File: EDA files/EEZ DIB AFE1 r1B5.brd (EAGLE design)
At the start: 141.5 x 68.5 mm, 198 parts, among them IC1 MCP6004T-I/ST, IC10 N.C., IC11 N.C., IC12 N.C., IC13 ADS131E04IPAGR, IC14 TPS71725DCKR, IC15 TPS72325DBVR, IC2 DG212BDY-T1-E3, IC3 ULN2803ADWR, IC4 MCP6004T-I/ST, IC5 DG212BDY-T1-E3, IC6 TLV9001IDBVR, IC7 DG212BDY-T1-E3, IC8 TLV9001IDBVR, IC9 DG212BDY-T1-E3, Q1 CPC3902ZTR, Q2 CPC3902ZTR, Q3 CPC3902ZTR, Q4 CPC3902ZTR, Q5 BSS214NH6327XTSA1, Q6 BSS214NH6327XTSA1, Q7 BSS214NH6327XTSA1, Q8 BSS214NH6327XTSA1, X1 691322310008, X2 DS1023-2*14S21, X3 DS1023-2*14S21

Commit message: #1, #2, BOM (r1B5)
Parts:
- removed C28A: N.C., EEZ_Lib1:C050-075X110
- removed C36, C37, C42, C47, C48: 1u, rcl:C0805
- removed C38, C39, C40, C41: 470p, rcl:C0603
- removed C43, C44, C45, C46, C49, C50, C51: 100n, rcl:C0603
- removed C52: 10u, rcl:C1206
- removed IC14: TPS71725DCKR, EEZ_TI:DCK5
- removed IC15: TPS72325DBVR, EEZ_TI:DBV5
- removed JP7: JP2-CUT-0805, EEZ_Lib1:R_0805
- removed R55, R56, R57, R58, R59, R60, R61: 1K, rcl:R0805
- removed R62, R63: 10K, rcl:R0805
- removed R64, R65: 10R, rcl:R1206
- added XO1: N.C., EEZ_DIB:XLH
- C12: value N.C. -> 10u; device rcl:C0805 -> rcl:C1206
- C17: value 470p -> 22u; device rcl:C0603 -> rcl:C1206
- C18: value 470p -> 10u; device rcl:C0603 -> rcl:C1206
- C19: value 470p -> N.C.; device rcl:C0603 -> EEZ_Lib1:EC1206
- C20: value 470p -> N.C.; device rcl:C0603 -> EEZ_Lib1:C050-075X110
- C21: value 22u -> 100n; device rcl:C1206 -> rcl:C0603
- C22: value 10u -> 100n; device rcl:C1206 -> rcl:C0603
- C23: value N.C. -> 1u; device rcl:C0603 -> rcl:C0805
- C24, C25: value N.C. -> 1u; device rcl:C1206 -> rcl:C0805
- C26, C27: value N.C. -> 100n; device rcl:C1206 -> rcl:C0603
- C28: value N.C. -> 100n; device EEZ_Lib1:EC1206 -> rcl:C0603
- C29: value N.C. -> 100n
- C30, C31: value 15n -> 1u; device rcl:C0603 -> rcl:C0805
- C32, C33: value 15n -> 100n
- C35: value 100n -> 10u; device rcl:C0603 -> rcl:C1206
- F3, F5: value ZH32 (10A) -> ZH32 (1.25A)
- F4, F6: value ZH32 (1A) -> ZH32 (10A)
- IC11: value N.C. -> ADS131E04IPAGR; device EEZ_TI:DBV5 -> EEZ_TI:PAG64
- IC12: value N.C. -> TPS71725DCKR; device EEZ_TI:SOIC127P600X175-8N -> EEZ_TI:DCK5
- IC13: value ADS131E04IPAGR -> TPS72325DBVR; device EEZ_TI:PAG64 -> EEZ_TI:DBV5
- R1, R18: value 47R -> 15R
- R33, R43: value 0R33 -> GMR100HTBFIR022; device rcl:R1210 -> EEZ_Lib1:R_2512-4WIRE
- R51, R52: value N.C. -> 10K
- R53: value N.C. -> 10R; device rcl:R0805 -> rcl:R1206
- R54: value 1K -> 10R; device rcl:R0805 -> rcl:R1206
- moved R53 41.7 mm to (73.9, 18.2), turned to 90 degrees
- moved C24 40.6 mm to (71.1, 14.7), turned to 180 degrees
- moved C25 39.6 mm to (77.0, 16.7)
- moved C26 39.5 mm to (77.4, 18.6), turned to 180 degrees
- moved C35 36.7 mm to (101.1, 27.8), turned to 0 degrees
- moved C28 36.1 mm to (82.9, 26.2), turned to 90 degrees
- moved C23 35.2 mm to (75.1, 14.7)
- moved IC12 34.3 mm to (74.8, 11.4)
- moved C8 32.6 mm to (117.2, 65.6), turned to 180 degrees
- moved C20 32.5 mm to (111.9, 14.1)
- moved C34 31.4 mm to (100.2, 25.8)
- moved C19 30.4 mm to (108.5, 9.03), turned to 180 degrees
- moved R51 25.2 mm to (82.0, 14.1), turned to 180 degrees
- moved C27 22.5 mm to (101.9, 24.1), turned to 0 degrees
- moved F3 22.2 mm to (47.9, 46.6)
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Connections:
- removed net IN1+: C20.2, C30.2, IC13.16, R54.2
- removed net IN1-: C19.2, C30.1, IC13.15, R55.2
- removed net IN2+: C18.2, C31.2, IC13.14, R56.2
- removed net IN2-: C17.2, C31.1, IC13.13, R57.2
- removed net IN3+: C32.2, C38.2, IC13.12, R58.2
- removed net IN3-: C32.1, C39.2, IC13.11, R59.2
- removed net IN4+: C33.2, C40.2, IC13.10, R60.2
- removed net IN4-: C33.1, C41.2, IC13.9, R61.2
- removed net N$100: C27.1, C28.+, C28A.1, IC10.6, IC10.7, IC12.6, JP5.NC, R53.2
- removed net N$101: C25.1, C26.1, IC11.3, R53.1
- removed net N$102: C12.2, IC11.4, R51.2
- removed net N$103: C12.1, IC11.1, R52.2
- removed net N$104: JP5.NO, R51.1, R52.1
- removed net N$141: F4.2, ISEL10A_1.14, ISEL10A_1.24
- removed net N$31: F6.2, ISEL10A_2.14, ISEL10A_2.24
- removed net N$37: F5.2, ISEL10A_2.11, ISEL10A_2.21
- new net N$2: F6.1, ISEL10A_2.12, ISEL10A_2.22
- new net N$32: IC9.15, R43.2S
- new net N$55: Q6.2, R31.1, R33.2
- new net N$97: JP6.NC, XO1.4
- net !ADC_CS: now also IC11.39; no longer IC13.39
- net !ADC_DRDY: now also IC11.47; no longer IC13.47
- net !RESET: now also IC11.36; no longer IC13.36
- net +2V5_ADC: now also C25.2, C26.1, C27.1, C28.1, C29.1, C30.2, IC11.19, IC11.21, IC11.22, IC11.54, IC11.56, IC11.59, R53.2; no longer C42.2, C43.1, C44.1, C45.1, C46.1, C47.2, IC13.19, IC13.21, IC13.22, IC13.54, IC13.56, IC13.59, R64.2
- net +2V5_ISO: now also C23.2, IC12.5, R53.1; no longer C36.2, IC14.5, R64.1
- net +3V3_ISO: now also C31.1, C32.2, C33.2, IC11.48, IC11.50, JP5.NC, R51.2, XO1.6; no longer C48.1, C49.2, C50.2, IC13.48, IC13.50, JP6.NC, R62.2
- net +5V_ISO: now also C12.1; no longer C23.1, C24.1, IC11.5, IC12.2
- net -2V5_ISO: now also IC13.5, R54.2; no longer C25.2, C26.2, C27.2, C28.-, C28A.2, C37.2, IC10.3, IC10.4, IC10.5, IC10.8, IC12.4, IC15.5, R65.2
- net -5V_ISO: no longer C29.2, IC11.2
- net ADC_CLK: now also JP6.NO; no longer JP7.1
- net ADC_MISO: now also IC11.43; no longer IC13.43
- net ADC_MOSI: now also IC11.34; no longer IC13.34
- net ADC_SCK: now also IC11.40; no longer IC13.40
- net ADC_START: now also IC11.38; no longer IC13.38
- net AIN3P: now also F4.2
- net AIN3P_FUSED: now also F3.1; no longer F4.1
- net AIN4P: now also F5.2, ISEL10A_2.11, ISEL10A_2.21; no longer F5.1
- net AIN4P_FUSED: now also F5.1; no longer F6.1
- net AVSS: now also C12.2, C17.1, C18.2, C19.-, C20.2, C25.1, C26.2, C29.2, C30.1, C34.1, C35.1, IC10.3, IC10.4, IC10.5, IC10.8, IC11.20, IC11.23, IC11.25, IC11.32, IC11.53, IC11.57, IC11.58, R54.1; no longer C21.1, C22.2, C42.1, C43.2, C46.2, C47.1, C51.1, C52.1, IC13.20, IC13.23, IC13.25, IC13.32, IC13.53, IC13.57, IC13.58, R65.1
- net GND: now also C21.2, C22.2, C23.1, C24.1, C27.2, C28.2, C31.2, C32.1, C33.1, IC11.31, IC11.33, IC11.41, IC11.49, IC11.51, IC12.2, IC13.1, JP5.NO, XO1.3; no longer C17.1, C18.1, C19.1, C20.1, C23.2, C29.1, C36.1, C37.1, C38.1, C39.1, C40.1, C41.1, C44.2, C45.2, C48.2, C49.1, C50.1, C51.2, C52.2, IC13.31, IC13.33, IC13.41, IC13.49, IC13.51, IC14.2, IC15.1, JP6.NO
- net HI_CURR#2: now also R33.1S
- net HI_CURR#4: now also F6.2, R43.1S; no longer ISEL10A_2.12, ISEL10A_2.22
- net IN1N: now also IC11.15; no longer R55.1
- net IN1P: now also IC11.16; no longer R54.1
- net IN2N: now also IC11.13; no longer R57.1
- net IN2P: now also IC11.14; no longer R56.1
- net IN3N: now also IC11.11; no longer R59.1
- net IN3P: now also IC11.12; no longer R58.1
- net IN4N: now also IC11.9; no longer R61.1
- net IN4P: now also IC11.10, IC9.10, IC9.14; no longer IC9.11, IC9.15, R60.1
- net ISEL_LOW#4: now also IC9.9; no longer IC9.16
- net ISEL_MID#4: now also IC9.16; no longer IC9.9
- net N$1: now also IC11.52, R52.1; no longer IC13.52, R63.1
- net N$14: now also JP5.COM, R52.2; no longer JP6.COM, R63.2
- net N$15: no longer IC9.10
- net N$17: now also IC9.11; no longer IC9.14
- net N$170: now also R33.2S; no longer Q6.2, R31.1, R33.2
- net N$3: now also C21.1, IC12.1, IC12.3; no longer C34.1, IC14.1, IC14.3
- net N$30: now also F4.1; no longer F3.1
- net N$9: now also C22.1, IC13.2, IC13.3; no longer C35.1, IC15.2, IC15.3
- net N$92: now also C17.2, IC11.28; no longer C21.2, IC13.28
- net N$93: now also IC11.30; no longer IC13.30
- net N$94: now also IC11.55; no longer IC13.55
- net N$95: now also IC11.26; no longer IC13.26
- net N$96: now also IC11.37, JP6.COM; no longer IC13.37, JP7.2
- net N$98: now also IC11.35, R51.1; no longer IC13.35, R62.1
- net VREFP: now also C18.1, C19.+, C20.1, IC10.6, IC10.7, IC11.24; no longer C22.1, IC13.24, JP5.COM
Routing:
- net -5V_ISO: track 106.5 -> 47.4 mm, vias 7 -> 4
- net N$100: track 51.1 -> 0.00 mm, vias 4 -> 0
- net HI_CURR#4: track 69.3 -> 41.1 mm, vias 2 -> 0
- net AIN3P: track 30.2 -> 54.1 mm
- net N$2: track 0.00 -> 23.4 mm
- net N$37: track 21.1 -> 0.00 mm
- net N$15: track 24.1 -> 6.17 mm, vias 3 -> 0
- net +5V_ISO: track 308.9 -> 291.0 mm, vias 20 -> 16
- net N$31: track 15.9 -> 0.00 mm
- net AIN4P: track 143.0 -> 158.3 mm
- net ISEL10A_R4_OUT: track 38.5 -> 23.3 mm
- net AIN4N: track 195.7 -> 180.6 mm, vias 15 -> 12
- net N$141: track 15.0 -> 0.00 mm
- net VREFP: track 42.3 -> 56.5 mm, vias 2 -> 1
- net IN1N: track 146.2 -> 160.4 mm
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- added copper zone on layer 16, net AIN3P
- added copper zone on layer 1, net HI_CURR#4
- added copper zone on layer 16, net N$2
- added copper zone on layer 1, net N$30
- removed copper zone on layer 1, net -2V5_ISO
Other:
- board size 141.5 x 68.5 mm -> 143 x 68.5 mm
- board text added: "AIN1+ AIN1- AIN2- AIN3+ AIN3- AIN4+ AIN4-"
- board text added: "AIN2+"
- board text added: "EEZ DIB AFE1 (05/2021 r1B5)"
- board text removed: "AIN1+ AIN1- AIN2+ AIN2- AIN3+ AIN3- AIN4+ AIN4-"
- board text removed: "EEZ DIB AFE1 (01/2021 r1B3)"

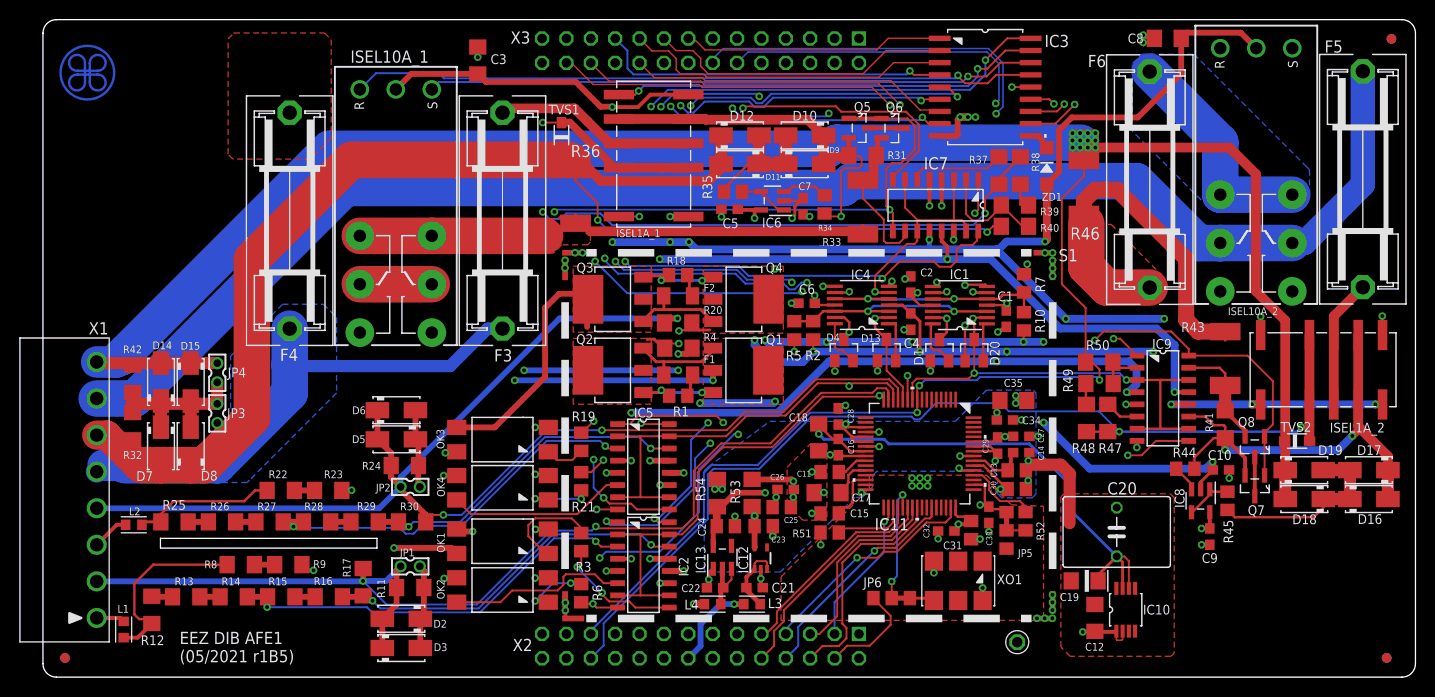
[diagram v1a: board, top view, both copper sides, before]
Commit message: New Rsense values, PCB layout adjustment for mid range Rsense
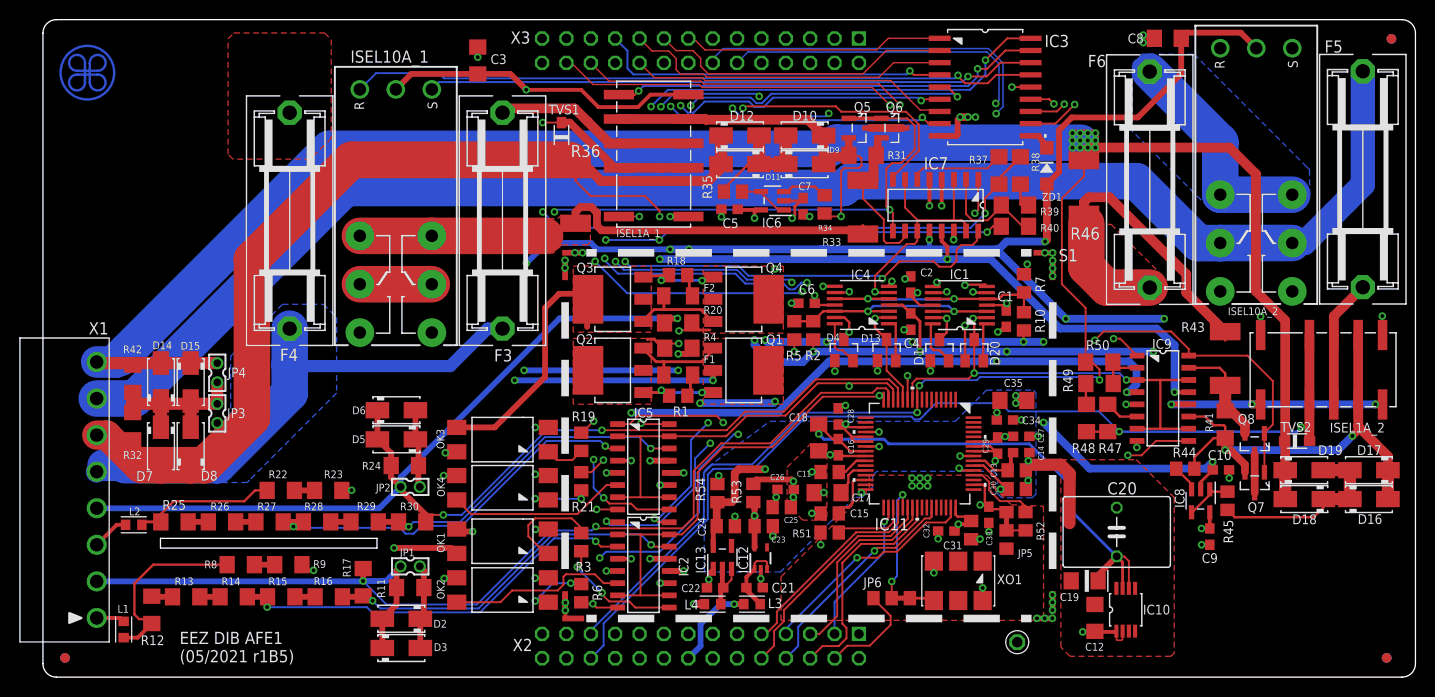
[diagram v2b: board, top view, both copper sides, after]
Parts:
- C12: value 10u -> N.C.
- R1, R18: value 15R -> 10R
- R20, R4: value 50R 0.1% -> 33R 0.1%
- R31, R41: value 33R -> 20R
- R53, R54: device rcl:R1206 -> rcl:R0805
- moved Q7 0.32 mm to (126.3, 19.3)
- moved Q8 0.32 mm to (126.3, 23.3)
- moved R53 0.13 mm to (74.0, 18.2)
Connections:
- new net N$31: R33.1, R33.1S, R36.2S
- new net N$37: R43.1, R43.1S, R46.2S
- net HI_CURR#2: no longer R33.1, R33.1S, R36.2S
- net HI_CURR#4: no longer R43.1, R43.1S, R46.2S
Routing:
- net N$31: track 0.00 -> 33.1 mm
- net HI_CURR#2: track 48.6 -> 19.3 mm
- net HI_CURR#4: track 41.1 -> 13.7 mm
- net N$37: track 0.00 -> 23.1 mm
- net +5V_ISO: track 291.0 -> 304.8 mm
- net IN3N: track 116.3 -> 123.3 mm, vias 3 -> 5
- net N$17: track 50.2 -> 49.0 mm
- net AVSS: track 35.6 -> 35.5 mm, vias 15 -> 14
